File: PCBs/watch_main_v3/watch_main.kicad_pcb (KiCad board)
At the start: 8 copper layers, 37 x 40.5 mm, 146 parts, among them IC1001 S26HS512TGABHI000, IC1101 NVT4858HKZ, IC1301 IIS2MDCTR, IC1302 OPT3004DNPR, IC1801 M24256X-FCU6T_VF, IC201 ADP5360ACBZ-2-R7, IC401 BGA725L6E6327FTSA1, J1101 105162-0001, J1701 10-Pin Pogo Connector, J501 AXG130144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

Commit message: Started watch_main_v3
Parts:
- removed C301, C302, C310, C311, C316: 1u, Capacitor_SMD:C_0402_1005Metric
- removed C303, C304, C305, C306, C308, C309, C312, C313, C314: 100n, Capacitor_SMD:C_0402_1005Metric
- removed C307: 2n2, Capacitor_SMD:C_0402_1005Metric
- removed C315: 0p7, Capacitor_SMD:C_0402_1005Metric
- removed L301, L302: 10u, Inductor_SMD:L_TDK_MLZ1608
- removed L303: 2n2, Inductor_SMD:L_0402_1005Metric
- removed TP301, TP302, TP303: 1.5mm, TestPoint:TestPoint_Pad_D1.5mm
- removed U301: NRF5340-QKAA-R7, watch_footprints:NRF5340-QKAA-R7_modified
- removed U801: STM32U5A9NJH6Q, watch_footprints:TFBGA216_13X13_STM
- removed Y301: 32MHz, Crystal:Crystal_SMD_2016-4Pin_2.0x1.6mm
- moved C901 32.3 mm to (167.4, 71.5)
- moved C903 32.3 mm to (170.5, 69.2)
- moved C905 32.3 mm to (170.5, 66.8)
- moved C907 32.3 mm to (167.0, 69.2)
- moved C908 32.3 mm to (168.0, 69.2)
- moved C910 32.3 mm to (169.0, 69.2)
- moved C911 32.3 mm to (165.0, 65.9)
- moved C918 32.3 mm to (165.0, 69.2)
- moved C920 32.3 mm to (166.2, 71.4)
- moved C902 32.3 mm to (167.0, 65.8)
- moved C904 32.3 mm to (168.7, 67.5)
- moved C909 32.3 mm to (169.0, 65.8)
- moved C913 32.3 mm to (166.0, 65.8)
- moved C914 32.3 mm to (168.0, 65.8)
- moved C917 32.3 mm to (165.3, 67.5)
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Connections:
- IC1001 pad A3: /Flash/CS2 -> unconnected-(IC1001-DNU_1-PadA3)
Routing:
- net /Micro SD/CD: track 60.0 -> 0.00 mm, vias 3 -> 0
- net /Micro SD/EN: track 58.2 -> 0.00 mm, vias 3 -> 0
- net /Expansion Connector/GPIO1: track 49.8 -> 0.00 mm, vias 2 -> 0
- net /Expansion Connector/GPIO2: track 49.1 -> 0.00 mm, vias 3 -> 0
- net /Bluetooth/SWD.RST: track 43.2 -> 0.00 mm, vias 2 -> 0
- net +1V8: track 71.0 -> 28.4 mm, vias 64 -> 25
- net /STM32/SWD.SWDIO: track 37.8 -> 0.00 mm, vias 2 -> 0
- net /USB.DN: track 37.2 -> 0.00 mm, vias 2 -> 0
- net /USB.DP: track 37.2 -> 0.00 mm, vias 2 -> 0
- net /STM32/SWD.SWCLK: track 37.1 -> 0.00 mm, vias 2 -> 0
- net /Bluetooth/UART_CTS: track 35.9 -> 0.00 mm, vias 2 -> 0
- net GND: track 101.5 -> 65.6 mm, vias 256 -> 177
- net /Bluetooth/SWD.SWDIO: track 35.5 -> 0.00 mm, vias 2 -> 0
- net /Flash/CS2: track 35.1 -> 0.00 mm, vias 3 -> 0
- net /STM32/SWO: track 33.3 -> 0.00 mm, vias 2 -> 0
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- removed copper zone on In2.Cu, net +1V8
- removed copper zone on In5.Cu, net +1V8
- removed copper zone on In5.Cu, net +3V3
- removed copper zone on B.Cu, net /Bluetooth/DECR
- removed copper zone on In5.Cu, net /STM32 Power/VDD11
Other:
- board text added: "1"
- board text added: "1 SWCLK 2 SWDIO 3 RST 4 GND 5 SWCLK 6 SWO 7 SWDIO 8 RST"
- board text added: "10"
- board text added: "15"
- board text added: "16"
- board text added: "19"
- board text added: "2"
- board text added: "20"
- board text added: "3"
- board text added: "30"
- board text added: "4"
- board text added: "5"
- board text added: "6"
- board text added: "7"
- board text added: "8"
- board text added: "G"
- board text added: "IO3"
- board text added: "Made by Ben Smith 2023"
- board text added: "NRF"
- board text added: "STM"
- board text added: "VBAT"
- board text added: "Watch Main Board v2.0"
- board text removed: "locked"

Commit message: watch_main_v3 updates
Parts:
- added REF**: BGA-144_12x12_10.0x10.0mm, watch_footprints:BGA-144_12x12_10.0x10.0mm, F.Cu at (149.2, 95.4)
- added REF**: LBEE5PK2AE-564, watch_footprints:LBEE5PK2AE-564, F.Cu at (142.7, 85.3)
- U101: footprint watch_footprints:Watch Outline V2 -> watch_footprints:Watch Outline V3
- moved C906 19.0 mm to (174.2, 88.3)
- moved C922 19.0 mm to (174.2, 87.3)
- moved R801 18.1 mm to (172.3, 82.0)
- moved R802 18.1 mm to (172.3, 81.0)
- moved R805 18.1 mm to (172.3, 79.0)
- moved R806 18.1 mm to (172.3, 80.0)
- moved R809 17.8 mm to (150.7, 124.2)
- moved R810 17.8 mm to (150.7, 123.2)
- moved C1101 16.6 mm to (175.8, 92.1)
- moved L901 16.6 mm to (173.7, 85.2)
- moved C1501 11.2 mm to (175.8, 94.7)
- moved C804 10.9 mm to (152.6, 101.4), turned to 135 degrees
- moved C803 10.1 mm to (150.0, 104.0), turned to 135 degrees
- moved Y802 9.86 mm to (151.3, 102.7), turned to -135 degrees
- moved R807 8.12 mm to (174.0, 95.4)
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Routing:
- net /STM32/BTN: track 35.1 -> 0.00 mm, vias 3 -> 0
- net /STM32/IMU_INT1: track 30.2 -> 8.45 mm, vias 2 -> 1
- net /SPI1.SCK: track 21.2 -> 0.00 mm, vias 2 -> 0
- net /SPI1.MISO: track 18.8 -> 0.00 mm, vias 2 -> 0
- net /SPI1.CS: track 19.8 -> 1.07 mm
- net /STM32/SWD.RST: track 18.4 -> 1.20 mm, vias 3 -> 1
- net /Micro SD/DAT2: track 16.6 -> 0.00 mm
- net /Micro SD/DAT3: track 16.5 -> 0.00 mm
- net /Micro SD/DAT0: track 16.3 -> 0.00 mm
- net /Micro SD/CLK: track 16.2 -> 0.00 mm
- net /STM32/IMU_INT2: track 17.6 -> 1.69 mm, vias 2 -> 1
- net /Micro SD/DAT1: track 15.9 -> 0.00 mm
- net /STM32/ALS_INT: track 15.4 -> 0.00 mm, vias 2 -> 0
- net /Micro SD/CMD: track 15.1 -> 0.00 mm, vias 2 -> 0
- net /STM32/TOUCH_RST: track 13.9 -> 0.00 mm, vias 1 -> 0
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- removed copper zone on B.Cu, net +1V8
- removed copper zone on F.Cu, net /Micro SD/+3V3_SD
- removed copper zone on B.Cu, net /STM32 Power/VDD11
- removed copper zone on B.Cu, net /STM32 Power/VLXSMPS
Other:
- board size 37 x 40.5 mm -> 37 x 42 mm
- board text added: "locked"
- board text removed: "10"
- board text removed: "15"
- board text removed: "16"
- board text removed: "30"

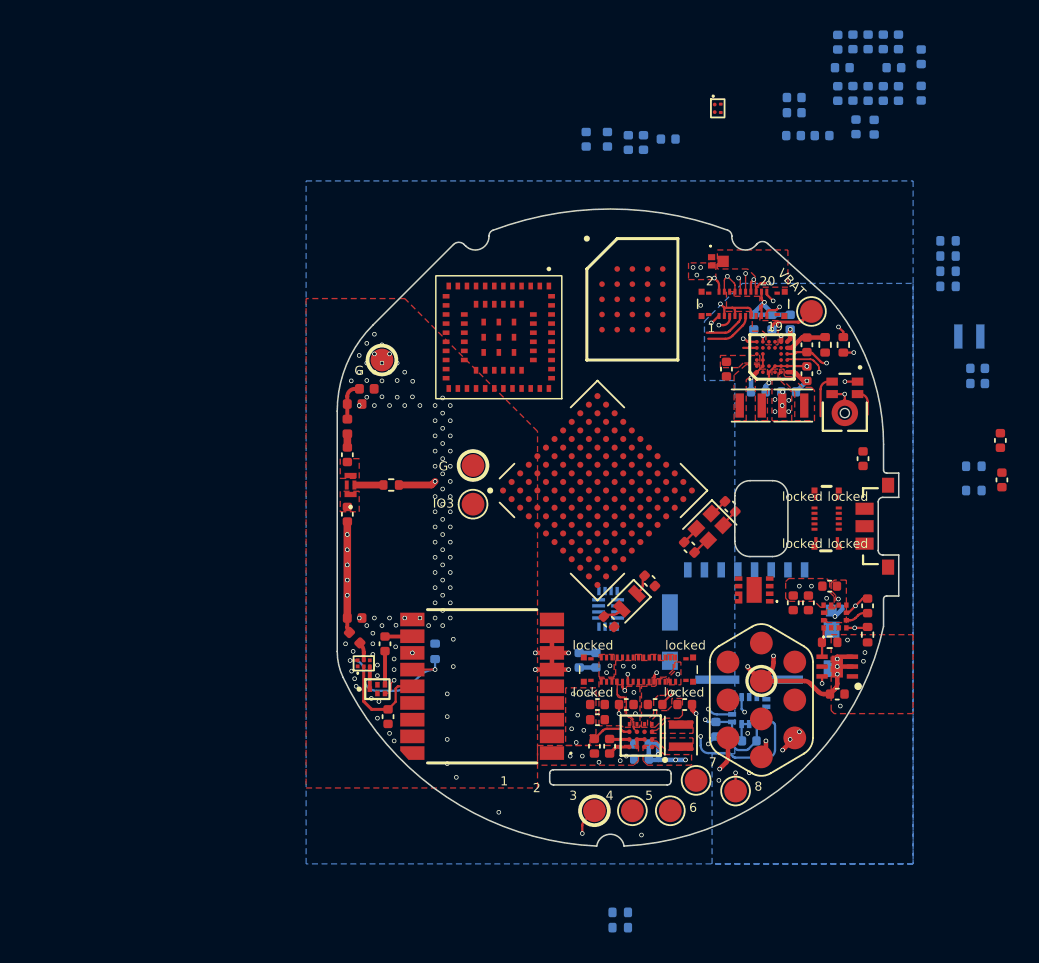
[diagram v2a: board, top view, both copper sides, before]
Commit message: watch_main_v3 updated layout
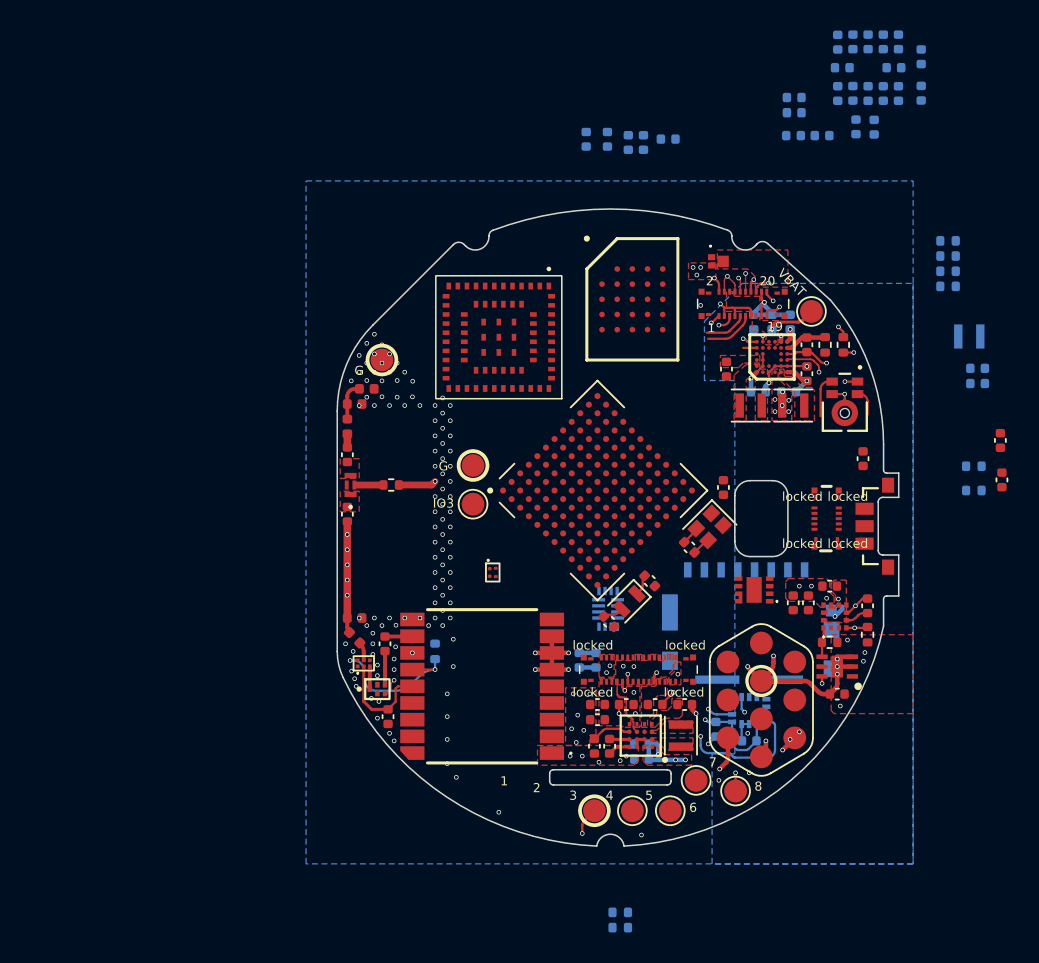
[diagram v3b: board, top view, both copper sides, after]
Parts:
- moved IC1801 34.0 mm to (142.3, 100.8)
- moved C802 1.33 mm to (157.5, 95.2), turned to -90 degrees
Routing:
- net GND: track 53.5 -> 52.4 mm
- net /STM32/OSC_OUT: track 1.23 -> 0.10 mm
- removed copper zone on In2.Cu, net GND
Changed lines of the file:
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@@
     (pad "M11" smd circle (at 3.6 4.4 45) (size 0.4 0.4) (layers "F.Cu" "F.Paste" "F.Mask"))
     (pad "M12" smd circle (at 4.4 4.4 45) (size 0.4 0.4) (layers "F.Cu" "F.Paste" "F.Mask"))
+    (model "${KIPRJMOD}/../component_library/watch_models/STM32U5G9ZJJ.stp"
+      (offset (xyz 0 0 0))
+      (scale (xyz 1 1 1))
+      (rotate (xyz 0 0 0))
+    )
   )
   (footprint "Capacitor_SMD:C_0402_1005Metric" (layer "F.Cu")
@@
   )
   (footprint "Capacitor_SMD:C_0402_1005Metric" (layer "F.Cu")
-    (at 157.943503 96.456497 135)
+    (at 157.5 95.2 -90)
     (descr "Capacitor SMD 0402 (1005 Metric), square (rectangular) end terminal, IPC_7351 nominal, (Body size source: IPC-SM-782 page 76, https://www.pcb-3d.com/wordpress/wp-content/uploads/ipc-sm-782a_amendment_1_and_2.pdf), generated with kicad-footprint-generator")
     (tags "capacitor")
@@
     (property "ki_keywords" "capacitor cap")
     (attr smd)
-    (fp_text reference "C802" (at 0 -1.16 135) (layer "F.SilkS") hide
+    (fp_text reference "C802" (at 0 -1.16 90) (layer "F.SilkS") hide
         (effects (font (size 1 1) (thickness 0.15)))
     )
-    (fp_text value "6p" (at 0 1.16 135) (layer "F.Fab")
+    (fp_text value "6p" (at 0 1.16 90) (layer "F.Fab")
         (effects (font (size 1 1) (thickness 0.15)))
     )
-    (fp_text user "${REFERENCE}" (at 0 0 135) (layer "F.Fab")
+    (fp_text user "${REFERENCE}" (at 0 0 90) (layer "F.Fab")
         (effects (font (size 0.25 0.25) (thickness 0.04)))
     )
@@
     (fp_line (start 0.5 0.25) (end -0.5 0.25)
       (stroke (width 0.1) (type solid)) (layer "F.Fab"))
-    (pad "1" smd roundrect (at -0.48 0 135) (size 0.56 0.62) (layers "F.Cu" "F.Paste" "F.Mask") (roundrect_rratio 0.25)
+    (pad "1" smd roundrect (at -0.48 0 270) (size 0.56 0.62) (layers "F.Cu" "F.Paste" "F.Mask") (roundrect_rratio 0.25)
       (net 3 "GND") (pintype "passive"))
-    (pad "2" smd roundrect (at 0.48 0 135) (size 0.56 0.62) (layers "F.Cu" "F.Paste" "F.Mask") (roundrect_rratio 0.25)
+    (pad "2" smd roundrect (at 0.48 0 270) (size 0.56 0.62) (layers "F.Cu" "F.Paste" "F.Mask") (roundrect_rratio 0.25)
       (net 78 "/STM32/OSC_OUT") (pintype "passive"))
     (model "${KICAD6_3DMODEL_DIR}/Capacitor_SMD.3dshapes/C_0402_1005Metric.wrl"
@@
   )
   (footprint "watch_footprints:BGA4C50P2X2_70X98X33" (layer "F.Cu")
-    (at 157.126 70.215)
+    (at 142.3 100.8)
     (descr "M24256X-FCU6T/VF*3")
     (tags "Integrated Circuit")
@@
   (segment (start 148.2 117.465685) (end 148.2 118) (width 0.15) (layer "F.Cu") (net 3))
   (segment (start 166.68 102.52) (end 167 102.52) (width 0.15) (layer "F.Cu") (net 3))
-  (segment (start 158.282914 96.795908) (end 157.483883 97.594939) (width 0.15) (layer "F.Cu") (net 3))
   (segment (start 162.32 86.28) (end 162.2 86.4) (width 0.15) (layer "F.Cu") (net 3))
   (segment (start 160.01 82.727157) (end 160.01 82.3) (width 0.15) (layer "F.Cu") (net 3))
@@
   (segment (start 155.595908 99.482914) (end 156.394939 98.683883) (width 0.15) (layer "F.Cu") (net 77))
   (segment (start 156.394939 98.683883) (end 156.493934 98.683883) (width 0.15) (layer "F.Cu") (net 77))
-  (segment (start 157.604092 96.117086) (end 156.805061 96.916117) (width 0.15) (layer "F.Cu") (net 78))
   (segment (start 156.805061 96.916117) (end 156.706066 96.916117) (width 0.15) (layer "F.Cu") (net 78))
   (via (at 156 111.6) (size 0.3) (drill 0.2) (layers "F.Cu" "B.Cu") (remove_unused_layers) (keep_end_layers) (zone_layer_connections) (net 80))
@@
     )
   )
-  (zone (net 3) (net_name "GND") (layers "F.Cu" "In2.Cu") (hatch edge 0.5)
-    (priority 2)
-    (connect_pads yes (clearance 0.2))
-    (min_thickness 0.2) (filled_areas_thickness no)
-    (fill yes (thermal_gap 0.2) (thermal_bridge_width 0.2))
-    (polygon
-      (pts
-        (xy 145.25 115)
-        (xy 145.25 91.5)
-        (xy 136.5 82.75)
-        (xy 130 82.75)
-        (xy 130 115)
-      )
-    )
-  )
   (zone (net 0) (net_name "") (layer "In1.Cu") (name "ANT_IN1_VOID") (hatch edge 0.5)
     (connect_pads (clearance 0))
@@
     (polygon
       (pts
-        (xy 140 89)
-        (xy 135 84)
-        (xy 130 84)
+        (xy 140 87)
+        (xy 130 87)
         (xy 130 116)
         (xy 140 116)

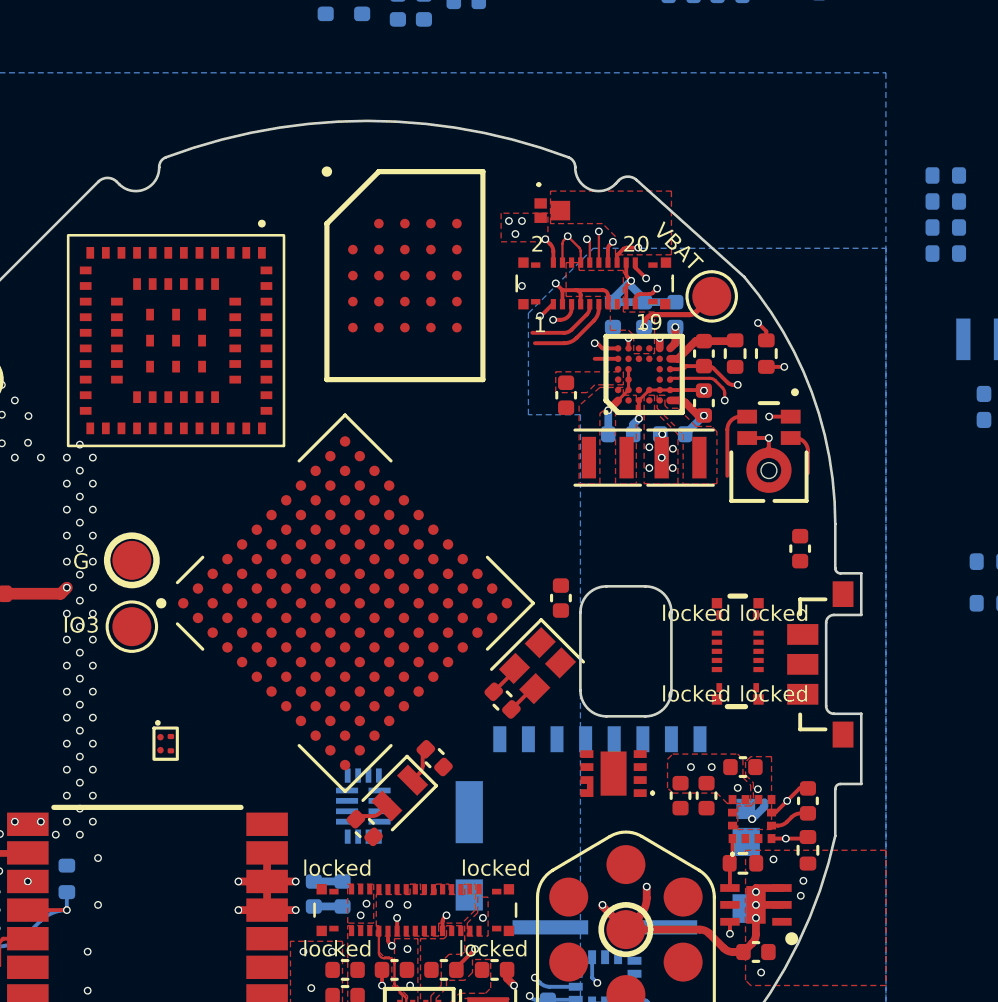
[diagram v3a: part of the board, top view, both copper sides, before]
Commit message: watch_main_v3 removed unnecessary capacitors from schematic.
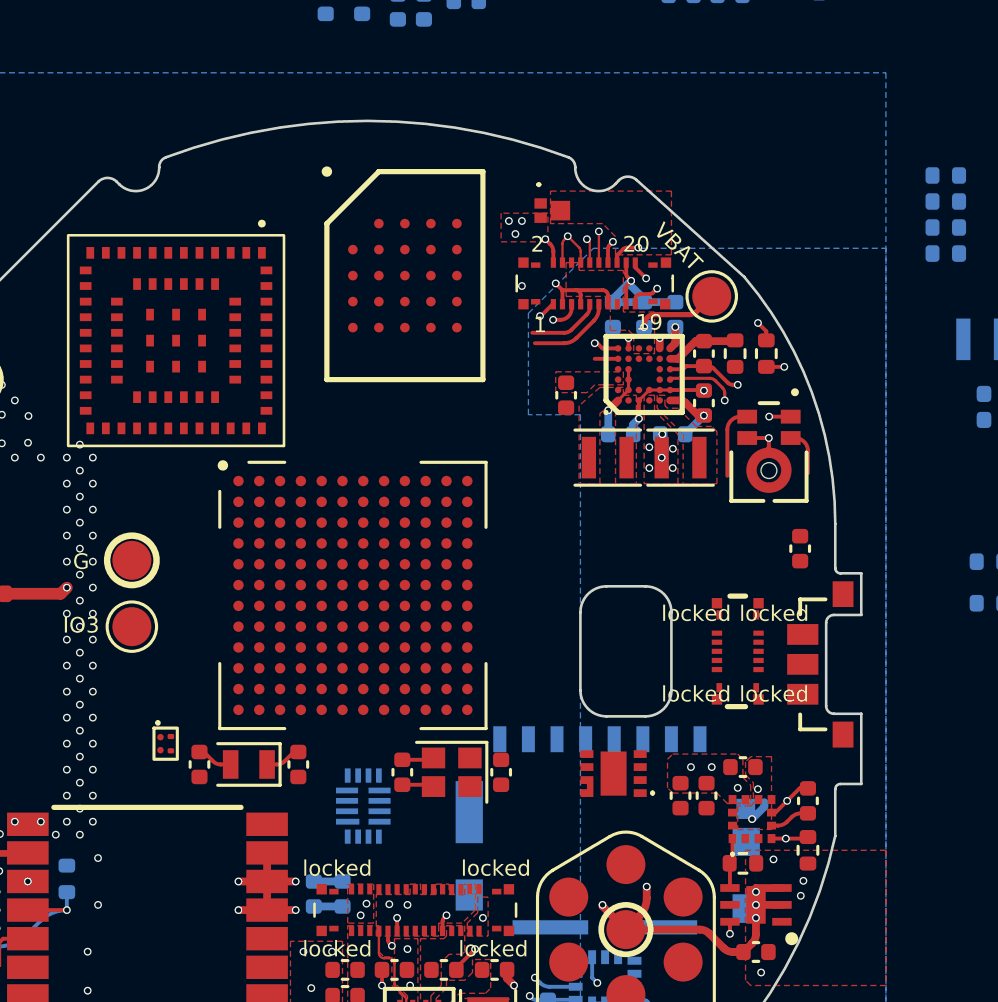
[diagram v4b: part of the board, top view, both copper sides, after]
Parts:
- moved C802 7.08 mm to (155.2, 101.9), turned to 90 degrees
- moved C803 6.81 mm to (143.6, 101.6), turned to 90 degrees
- moved Y802 5.90 mm to (145.5, 101.6), turned to 180 degrees
- moved Y801 5.26 mm to (153.3, 101.9), turned to 180 degrees
- moved C804 5.25 mm to (147.4, 101.6), turned to 90 degrees
- moved C801 4.74 mm to (151.4, 101.9), turned to -90 degrees
- moved REF** 0.42 mm to (149.5, 95.1), turned to 0 degrees

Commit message: watch_main_v3 WiFi/Bluetooth schematic done
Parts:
- removed C913, C917, C918: 100n, Capacitor_SMD:C_0402_1005Metric
- removed the REF** at (142.7, 85.3)
- removed U1102: NCP45525IMNTWG-H, watch_footprints:NCP45525IMNTWGH
- added C301: 10u, Capacitor_SMD:C_0402_1005Metric, F.Cu at (143.1, 80.1)
- added C302: 4u7, Capacitor_SMD:C_0402_1005Metric, B.Cu at (147.1, 82.2)
- added C303: 100n, Capacitor_SMD:C_0402_1005Metric, F.Cu at (145.1, 80.1)
- added C306: 10u, Capacitor_SMD:C_0402_1005Metric, F.Cu at (147.1, 80.1)
- added C307: 100n, Capacitor_SMD:C_0402_1005Metric, F.Cu at (147.6, 83.8)
- added IC1102: LQ05041QCS6, watch_footprints:BGA6C50P2X3_97X147X60, F.Cu at (159.2, 102.5)
- added IC301: LQ05041QCS6, watch_footprints:BGA6C50P2X3_97X147X60, F.Cu at (146.8, 78.7)
- added IC302: LQ05041QCS6, watch_footprints:BGA6C50P2X3_97X147X60, F.Cu at (144.4, 78.7)
- added L301: 2u2, Inductor_SMD:L_Murata_DFE201610P, B.Cu at (145.4, 82.2)
- added R301: 47k, Resistor_SMD:R_0402_1005Metric, F.Cu at (119.5, 96.5)
- added R302: 47k, Resistor_SMD:R_0402_1005Metric, F.Cu at (119.5, 98.5)
- added R303: 47k, Resistor_SMD:R_0402_1005Metric, F.Cu at (119.5, 100.5)
- added R304: 47k, Resistor_SMD:R_0402_1005Metric, F.Cu at (119.5, 102.5)
- added R305: 47k, Resistor_SMD:R_0402_1005Metric, F.Cu at (119.5, 104.5)
- added R811: 4k7, Resistor_SMD:R_0402_1005Metric, F.Cu at (112.6, 109.6)
- added R812: 4k7, Resistor_SMD:R_0402_1005Metric, F.Cu at (112.6, 111.6)
- added TP301: 1.5mm, TestPoint:TestPoint_Pad_D1.5mm, F.Cu at (116.3, 97.3)
- added TP302: 1.5mm, TestPoint:TestPoint_Pad_D1.5mm, F.Cu at (116.3, 100.9)
- added TP303: 1.5mm, TestPoint:TestPoint_Pad_D1.5mm, F.Cu at (116.3, 104.4)
- added U301: LBEE5PK2AE_564, watch_footprints:LBEE5PK2AE-564, F.Cu at (142.5, 85.0)
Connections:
- net /SDMMC1.CKIN renamed /Micro SD/SDIO.CKIN
- net /SPI1.CS renamed /SPIx.CS
- net /SPI1.MISO renamed /SPIx.MISO
- net /SPI1.MOSI renamed /SPIx.MOSI
- net /SPI1.SCK renamed /SPIx.SCK
- IC1301 pad 1: /I2C3.SCL -> /I2Cx.SCL
- IC1301 pad 4: /I2C3.SDA -> /I2Cx.SDA
- IC1302 pad 4: /I2C3.SCL -> /I2Cx.SCL
- IC1302 pad 6: /I2C3.SDA -> /I2Cx.SDA
- IC1801 pad A2: /I2C4.SCL -> /EEPROM/I2C.SCL
- IC1801 pad B1: /I2C4.SDA -> /EEPROM/I2C.SDA
- IC201 pad A4: /I2C2.SCL -> /I2Cx.SCL
- IC201 pad A5: /I2C2.SDA -> /I2Cx.SDA
- J1701 pad B1: /USART6.RX -> /USARTx.RX
- J1701 pad C1: /USART6.TX -> /USARTx.TX
- J501 pad 20: /I2C6.SCL -> /I2Cx.SCL
- J501 pad 21: /I2C6.SDA -> /I2Cx.SDA
- J601 pad 4: /I2C1.SDA -> /I2Cx.SDA
- J601 pad 5: /I2C1.SCL -> /I2Cx.SCL
- J701 pad 11: /I2C4.SDA -> /I2Cx.SDA
- J701 pad 9: /I2C4.SCL -> /I2Cx.SCL
- R801 pad 1: +1V8 -> Net-(R801-Pad1)
- R801 pad 2: /I2C2.SCL -> /STM32/I2C2.SCL
- R802 pad 1: +1V8 -> Net-(R801-Pad1)
- R802 pad 2: /I2C2.SDA -> /STM32/I2C2.SDA
- R803 pad 1: +1V8 -> Net-(R803-Pad1)
- R803 pad 2: /I2C3.SCL -> /STM32/I2C3.SCL
- R804 pad 1: +1V8 -> Net-(R803-Pad1)
- R804 pad 2: /I2C3.SDA -> /STM32/I2C3.SDA
- R805 pad 1: +1V8 -> Net-(R805-Pad1)
- R805 pad 2: /I2C4.SCL -> /STM32/I2C4.SCL
- R806 pad 1: +1V8 -> Net-(R805-Pad1)
- R806 pad 2: /I2C4.SDA -> /STM32/I2C4.SDA
- R807 pad 1: +3V3 -> Net-(R807-Pad1)
- R807 pad 2: /I2C1.SCL -> /STM32/I2C1.SCL
- R808 pad 1: +3V3 -> Net-(R807-Pad1)
- R808 pad 2: /I2C1.SDA -> /STM32/I2C1.SDA
- R809 pad 1: +1V8 -> Net-(R809-Pad1)
- R809 pad 2: /I2C6.SCL -> /STM32/I2C5.SCL
- R810 pad 1: +1V8 -> Net-(R809-Pad1)
- R810 pad 2: /I2C6.SDA -> /STM32/I2C5.SDA
- U401 pad 2: /USART1.RX -> /USARTx.RX
- U401 pad 3: /USART1.TX -> /USARTx.TX
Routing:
- net /I2Cx.SDA: track 0.00 -> 4.17 mm
- net /I2C4.SDA: track 3.27 -> 0.00 mm
- net /I2Cx.SCL: track 0.00 -> 2.79 mm
- net /I2C4.SCL: track 2.79 -> 0.00 mm
- net /I2C2.SDA: track 0.90 -> 0.00 mm
- net GND: vias 148 -> 147
- net /WiFi and Bluetooth/WL_REG_EN: vias 0 -> 1
